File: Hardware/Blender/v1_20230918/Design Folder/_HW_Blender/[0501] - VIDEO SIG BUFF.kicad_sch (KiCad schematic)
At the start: 6 parts, among them U1201 MIC920YC5-TR

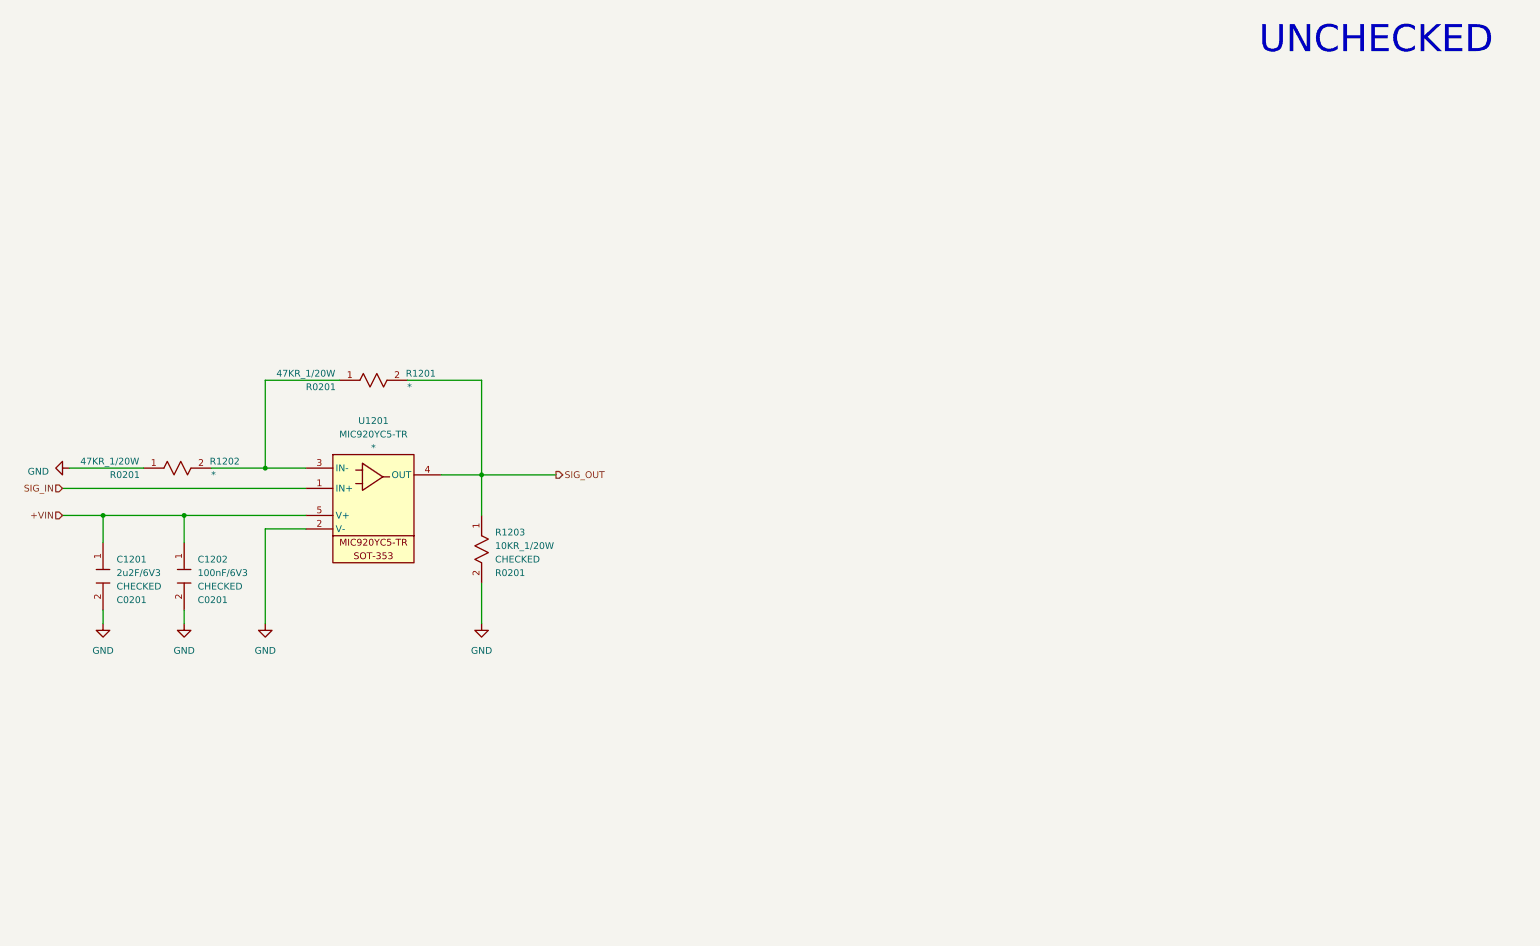
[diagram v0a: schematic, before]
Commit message: Improving the file structure and documentation
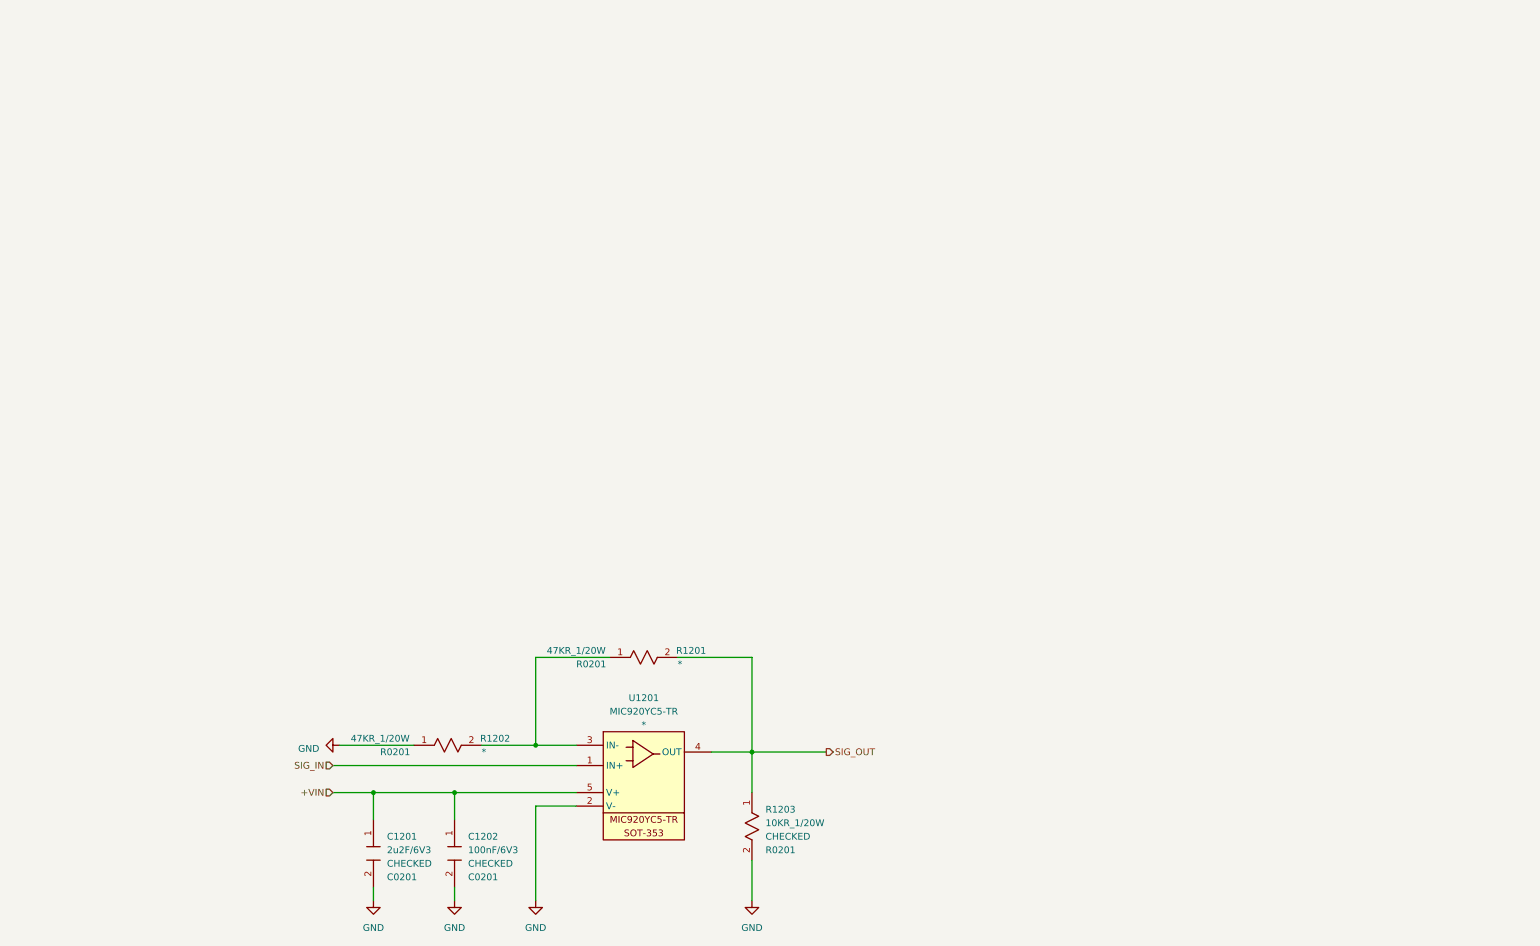
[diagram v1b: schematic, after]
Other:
- note removed: "UNCHECKED"
- moved on the sheet: C1201, C1202, R1201, R1202, R1203, U1201

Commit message: More update for hardware part
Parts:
- C1201: value 2u2F/6V3 -> 2u2F_6V3_X5R; symbol _SCHLIB_Blender:CAP_2u2F/6V3_C0201 -> _SCHLIB_Blender:CAP_2u2F_6V3_X5R_C0201; Manufacturer (none) -> KYOCERA AVX; PCB CHECk (none) -> PCB (N/A); Part Number CM03X5R225M06AH -> (none); Part Number (Manufacturer) (none) -> CM03X5R225M06AH; Part Number (Vendor) (none) -> 478-KGM03CR50J225MHTR-ND; SCH CHECK CHECKED -> SCH (N/A); Vendor (none) -> Digikey
- C1202: value 100nF/6V3 -> 100nF_6V3_X7R; symbol _SCHLIB_Blender:CAP_100nF/6V3_C0201 -> _SCHLIB_Blender:CAP_100nF_6V3_X7R_C0201; Manufacturer (none) -> YAGEO; PCB CHECk (none) -> PCB (N/A); Part Number CC0201KRX7R5BB104 -> (none); Part Number (Manufacturer) (none) -> CC0201KRX7R5BB104; Part Number (Vendor) (none) -> 13-CC0201KRX7R5BB104TR-ND; SCH CHECK CHECKED -> SCH (N/A); Vendor (none) -> Digikey
- R1201, R1202: value 47KR_1/20W -> 4K7R_1/20W_1%; symbol _SCHLIB_Blender:RES_47KR_1/20W_R0201 -> _SCHLIB_Blender:RES_4K7R_1/20W_1%_R0201; Link https://www.digikey.ca/en/products/detail/yageo/AC0201FR-07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 -> https://www.digikey.ca/en/products/detail/stackpole-electro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; Manufacturer (none) -> Stackpole Electronics Inc; PCB CHECk (none) -> PCB (N/A); Part Number AC0201FR-0747KL -> (none); Part Number (Manufacturer) (none) -> RMCF0201FT4K70; Part Number (Vendor) (none) -> RMCF0201FT4K70TR-ND; SCH CHECK * -> SCH (N/A); Vendor (none) -> Digikey
- R1203: value 10KR_1/20W -> 10KR_1/20W_1%; symbol _SCHLIB_Blender:RES_10KR_1/20W-R0201 -> _SCHLIB_Blender:RES_10KR_1/20W_1%_R0201; Manufacturer (none) -> Stackpole Electronics Inc; PCB CHECk (none) -> PCB (N/A); Part Number RMCF0201FT10K0 -> (none); Part Number (Manufacturer) (none) -> RMCF0201FT10K0; Part Number (Vendor) (none) -> RMCF0201FT10K0TR-ND; SCH CHECK CHECKED -> SCH (N/A); Vendor (none) -> Digikey
- U1201: symbol _SCHLIB_ToslinkToDMX:OPAMP_MIC920YC5-TR -> _SCHLIB_Blender:IC_OPAMP_MIC920YC5-TR_GP_1C_5V~18V_SC-70-5; Manufacturer (none) -> Microchip Technology; PCB CHECk (none) -> PCB (N/A); Package (none) -> SC-70-5; Part Number MIC920YC5-TR -> (none); Part Number (Manufacturer) (none) -> MIC920YC5-TR; Part Number (Vendor) (none) -> 576-4560-2-ND; SCH CHECK * -> SCH (N/A); Vendor (none) -> Digikey
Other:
- moved on the sheet: C1201, C1202, R1201, R1202, R1203, U1201
